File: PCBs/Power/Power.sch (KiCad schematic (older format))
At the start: 10 parts, among them J1 Power In, J2 Corner 1, J3 Corner 2, J4 Corner 3, J5 Corner 4, J6 Flight Controller

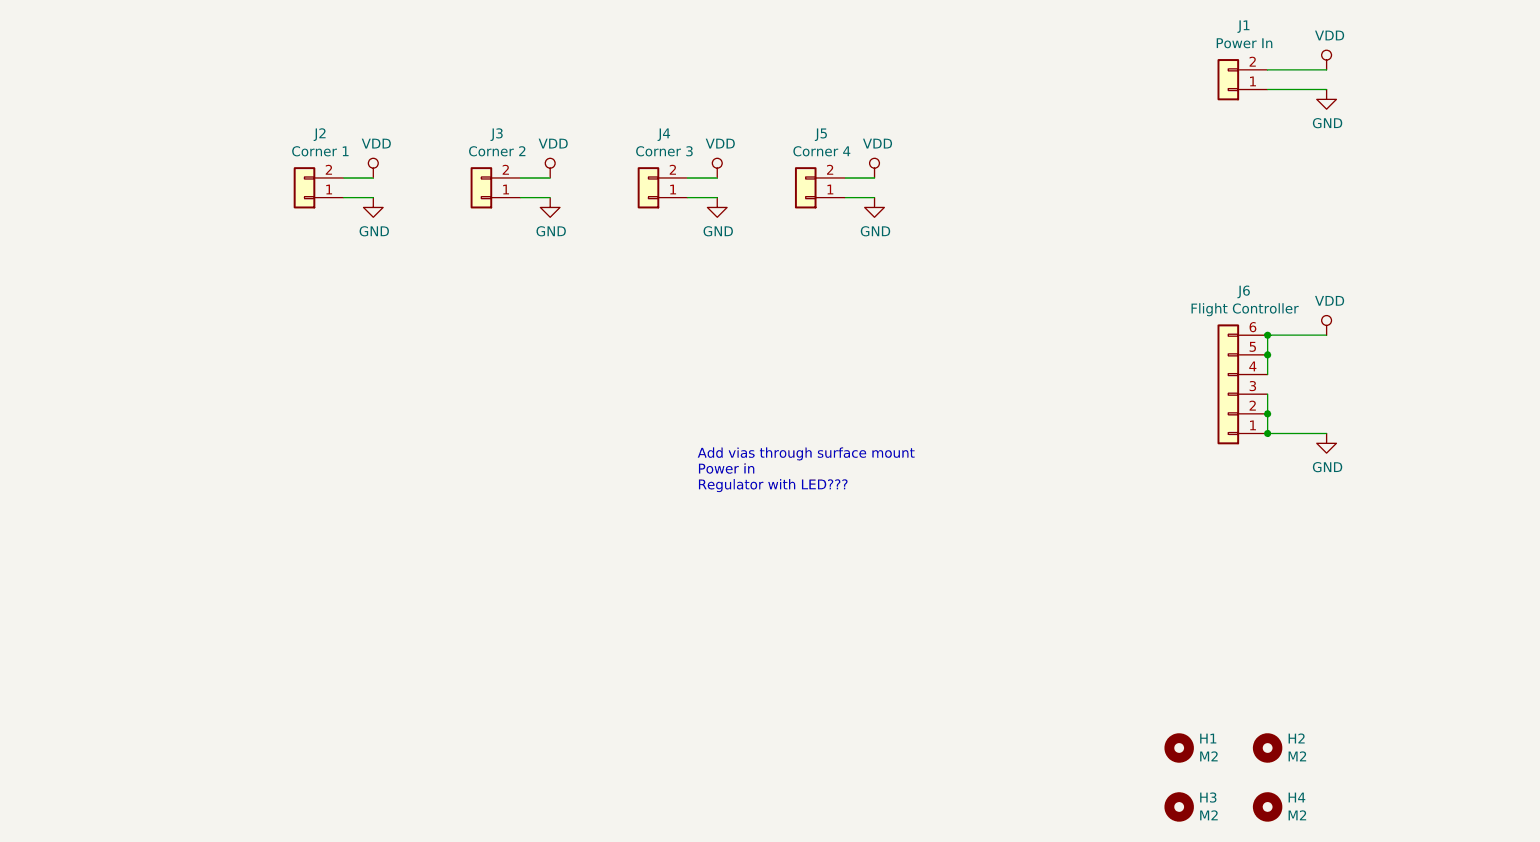
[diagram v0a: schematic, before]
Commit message: all footprints complete
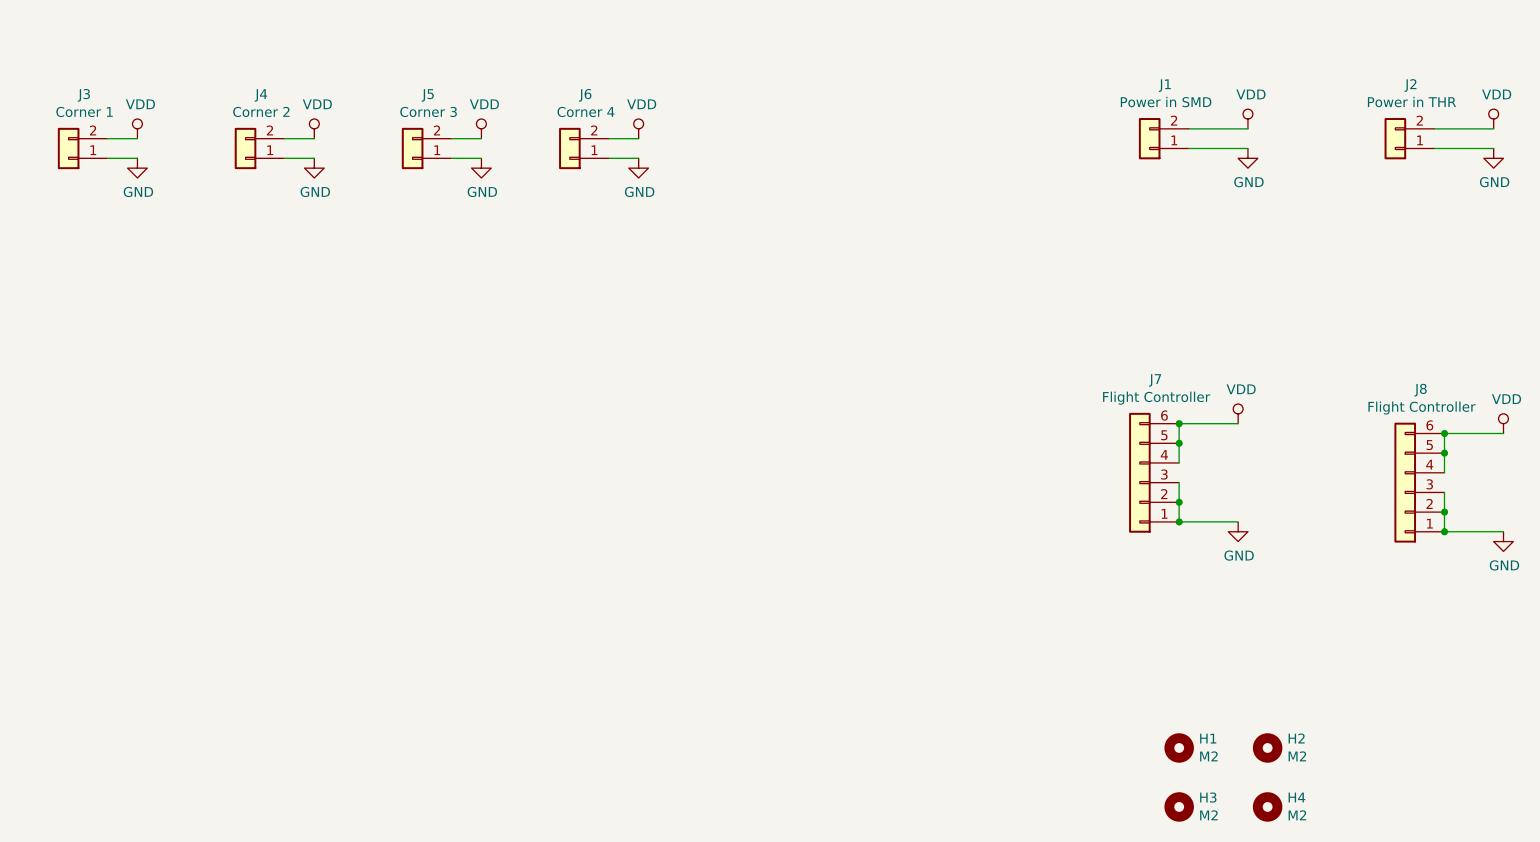
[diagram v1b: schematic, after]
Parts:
- added J2: Power in THR, Custom:THR-Power, symbol Connector_Generic:Conn_01x02
- added J7: Flight Controller, Connector_JST:JST_GH_BM06B-GHS-TBT_1x06-1MP_P1.25mm_Vertical, symbol Connector_Generic:Conn_01x06
- J1: value Power In -> Power in SMD; footprint (none) -> Custom:SMD-Power
- renumbered J2 to J3, J3 to J4, J4 to J5, J5 to J6, J6 to J8
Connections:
- net GND: now also J2.1 (Pin_1), J7.1 (Pin_1), J7.2 (Pin_2), J7.3 (Pin_3)
- net VDD: now also J2.2 (Pin_2), J7.4 (Pin_4), J7.5 (Pin_5), J7.6 (Pin_6)
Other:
- note removed: "Add vias through surface mount\nPower in \nRegulator with LED???"
- moved on the sheet: J1, J3, J4, J5, J6, J8

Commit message: Board complete
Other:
- note added: "Battery In"
- note added: "ESC Power"
- note added: "Flight Controller Power"
- note added: "Mounting Holes"
- moved on the sheet: H1, H2, H3, H4, J1, J2, J3, J4, J5, J6, J7, J8

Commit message: Update part numbers and create BOM
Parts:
- J7: Digi-Key # (none) -> 455-1582-1-ND; Manufacturer (none) -> JST Sales America Inc.; Manufacturer # (none) -> BM06B-GHS-TBT(LF)(SN)(N)
- J8: Digi-Key # (none) -> 455-1568-1-ND; Manufacturer (none) -> JST Sales America Inc.; Manufacturer # (none) -> SM06B-GHS-TB(LF)(SN)
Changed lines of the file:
@@
 EESchema Schematic File Version 4
+LIBS:Power-cache
 EELAYER 30 0
 EELAYER END
@@
 F 2 "Connector_JST:JST_GH_SM06B-GHS-TB_1x06-1MP_P1.25mm_Horizontal" H 8350 4900 50  0001 C CNN
 F 3 "~" H 8350 4900 50  0001 C CNN
+F 4 "JST Sales America Inc." H 8350 4900 50  0001 C CNN "Manufacturer"
+F 5 "SM06B-GHS-TB(LF)(SN)" H 8350 4900 50  0001 C CNN "Manufacturer #"
+F 6 "455-1568-1-ND" H 8350 4900 50  0001 C CNN "Digi-Key #"
 	1    8350 4900
 	-1   0    0    1
@@
 F 1 "Flight Controller" H 6918 4416 50  0000 C CNN
 F 2 "Connector_JST:JST_GH_BM06B-GHS-TBT_1x06-1MP_P1.25mm_Vertical" H 7000 4850 50  0001 C CNN
-F 3 "~" H 7000 4850 50  0001 C CNN
+F 3 "" H 7000 4850 50  0001 C CNN
+F 4 "JST Sales America Inc." H 7000 4850 50  0001 C CNN "Manufacturer"
+F 5 "BM06B-GHS-TBT(LF)(SN)(N)" H 7000 4850 50  0001 C CNN "Manufacturer #"
+F 6 "455-1582-1-ND" H 7000 4850 50  0001 C CNN "Digi-Key #"
 	1    7000 4850
 	-1   0    0    1
